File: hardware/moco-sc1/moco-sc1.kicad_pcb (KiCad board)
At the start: 6 copper layers, 40 x 40 mm, 118 parts, among them J1 Debug, J2 CAN, J3 CAN, J4 V+, J5 V-, J6 A, J7 B, J8 C, Q1 CSD88584Q5DC, Q2 CSD88584Q5DC, Q3 CSD88584Q5DC, SW1 RESET, U1 STSPIN32G4, U2 TCAN337, U3 MA702, Y1 16MHz

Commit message: Update parts
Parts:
- D1: value STPS0560Z -> MBR180S1
- J2, J3: footprint Connector_JST:JST_SH_SM03B-SRSS-TB_1x03-1MP_P1.00mm_Horizontal -> Connector_JST:JST_GH_SM03B-GHS-TB_1x03-1MP_P1.25mm_Horizontal
- L1: footprint Inductor_SMD:L_Sunlord_SWPA3012S -> Inductor_SMD:L_Neosid_SMS-ME3015
- U2: footprint Package_TO_SOT_SMD:SOT-23-8 -> Package_SO:SOIC-8_3.9x4.9mm_P1.27mm
- moved C1 2.40 mm to (105.5, 50.0)
- moved TP1 1.63 mm to (95.5, 47.8)
- moved SW1 1.25 mm to (91.8, 57.8)
- moved R1 1.13 mm to (96.8, 50.8)
- moved J2 0.96 mm to (93.0, 50.8)
- moved J3 0.96 mm to (93.0, 50.8)
- moved U2 0.90 mm to (101.2, 50.0)
- moved SB1 0.78 mm to (98.0, 52.2)
- moved TP2 0.72 mm to (95.5, 53.8)
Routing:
- net GND: track 48.2 -> 54.8 mm, vias 108 -> 107
- net /CANH: track 16.6 -> 21.0 mm
- net /CAN_TX: track 17.0 -> 15.4 mm
- net /CAN_RX: track 19.7 -> 18.4 mm
- net /CANL: track 11.2 -> 12.3 mm
- net /~{RESET}: track 19.3 -> 18.7 mm

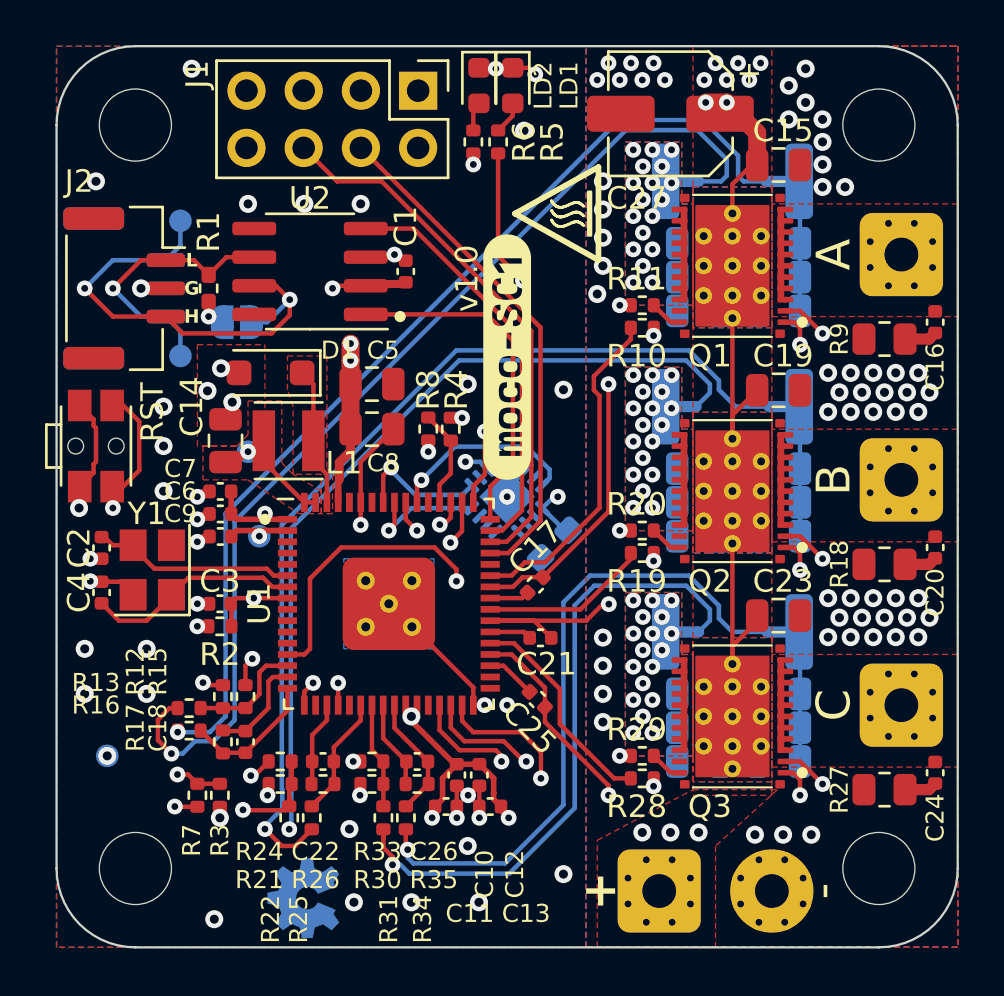
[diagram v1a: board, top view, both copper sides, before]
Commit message: Change to 4 layers board
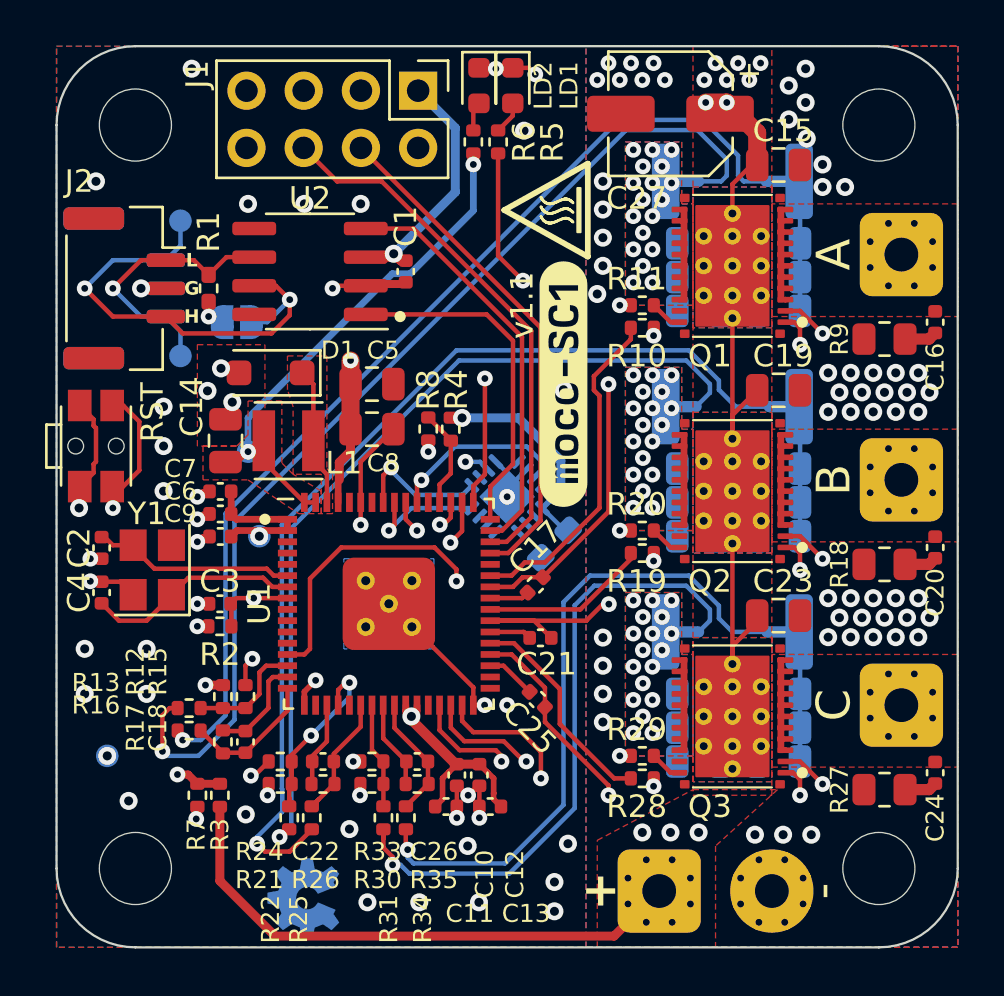
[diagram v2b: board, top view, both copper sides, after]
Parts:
- moved kibuzzard-64C58EFF 2.77 mm to (112.5, 55.0)
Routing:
- net +3.3V: track 25.8 -> 95.2 mm, vias 12 -> 9
- net /OPAMP2_VINP: track 14.2 -> 8.76 mm
- net VCC: track 25.5 -> 23.9 mm
- net /Power Stage/RSB-: track 42.6 -> 43.7 mm
- net /Power Stage/RSB+: track 36.8 -> 37.9 mm
- net GND: track 54.8 -> 54.3 mm, vias 107 -> 108
- net VBUS: vias 14 -> 12
- added copper zone on In1.Cu, net VBUS
- added copper zone on In2.Cu, net VBUS
- removed copper zone on In3.Cu, net +3.3V
- removed copper zone on In3.Cu, net /Power Stage/S2A
- removed copper zone on In4.Cu, net /Power Stage/S2A
- removed copper zone on In3.Cu, net /Power Stage/S2B
- removed copper zone on In4.Cu, net /Power Stage/S2B
- removed copper zone on In3.Cu, net /Power Stage/S2C
- removed copper zone on In4.Cu, net /Power Stage/S2C
- removed copper zone on In4.Cu, net GND
- removed copper zone on In3.Cu, net VBUS
- removed copper zone on In4.Cu, net VBUS
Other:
- copper layers 6 -> 4
- board text added: "GND PWR"
- board text added: "SIGNAL"
